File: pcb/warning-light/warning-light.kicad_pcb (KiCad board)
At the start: 2 copper layers, 80 x 80 mm, 14 parts, among them J1 01x02_12V_PWR_in, J2 Conn_02x20_Odd_Even, J3 01x02_relay_conn, U1 L7805CDT-TR, U2 relay

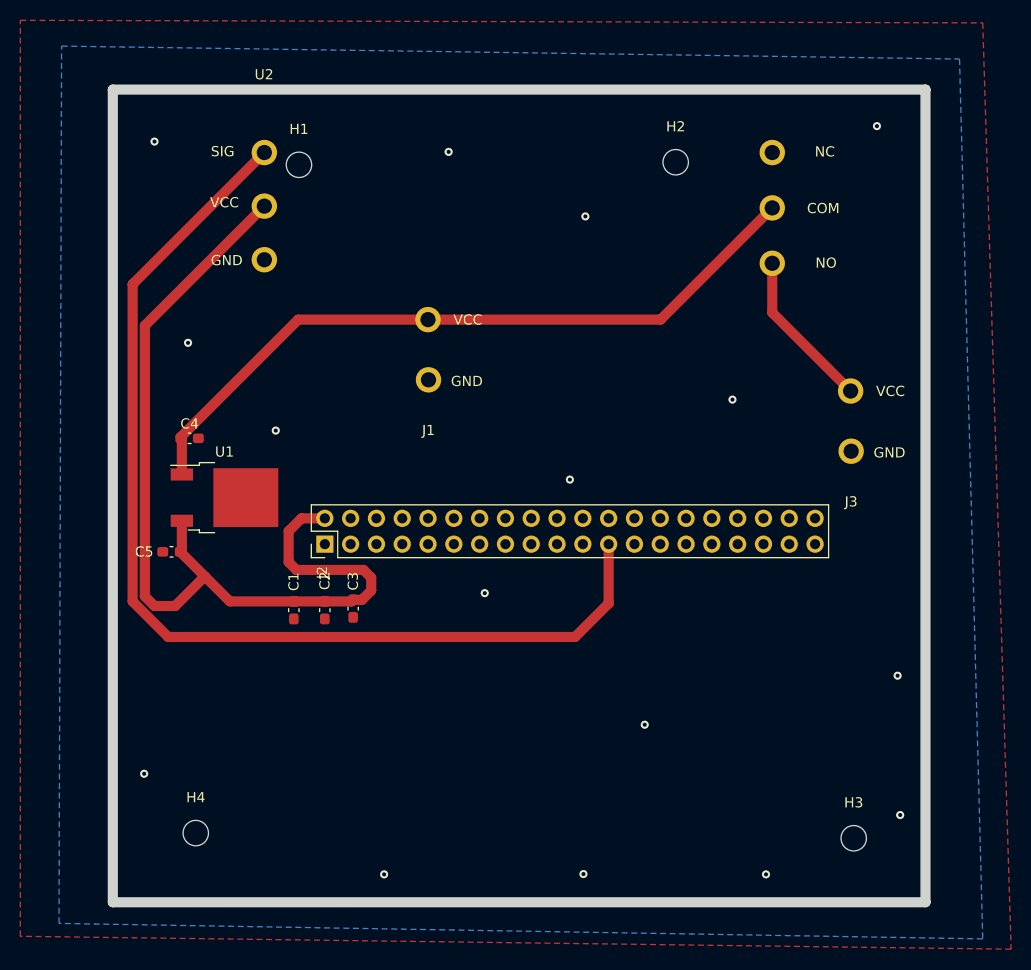
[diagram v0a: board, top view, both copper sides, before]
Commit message: finalize acrylic cuts for chassis
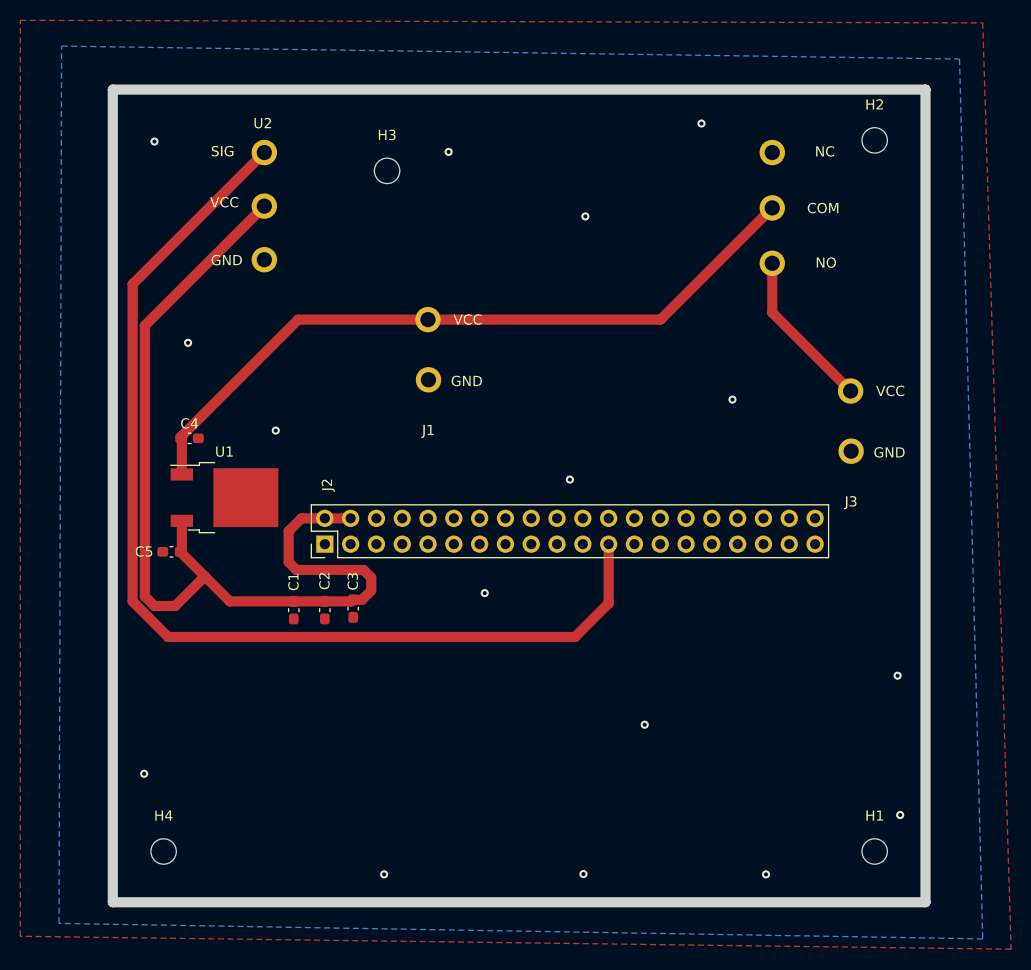
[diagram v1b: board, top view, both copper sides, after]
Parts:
- moved H1 88.2 mm to (125.0, 125.0)
- moved H3 80.2 mm to (77.0, 58.0)
- moved H2 19.7 mm to (125.0, 55.0)
- moved H4 3.65 mm to (55.0, 125.0)
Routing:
- net /5VDC_REG: track 92.3 -> 94.9 mm
